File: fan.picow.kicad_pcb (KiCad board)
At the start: 2 copper layers, 96.5 x 70.6 mm, 61 parts, among them J1 12v Input, J12 Temp, J2 Fan1, J3 Fan2, J4 Fan4, J5 Fan3, J7 OLED, Q1 BSS138, Q2 BSS138, Q3 IRLML9301, SW1 EG1257, U1 PicoW, U3 LM2575

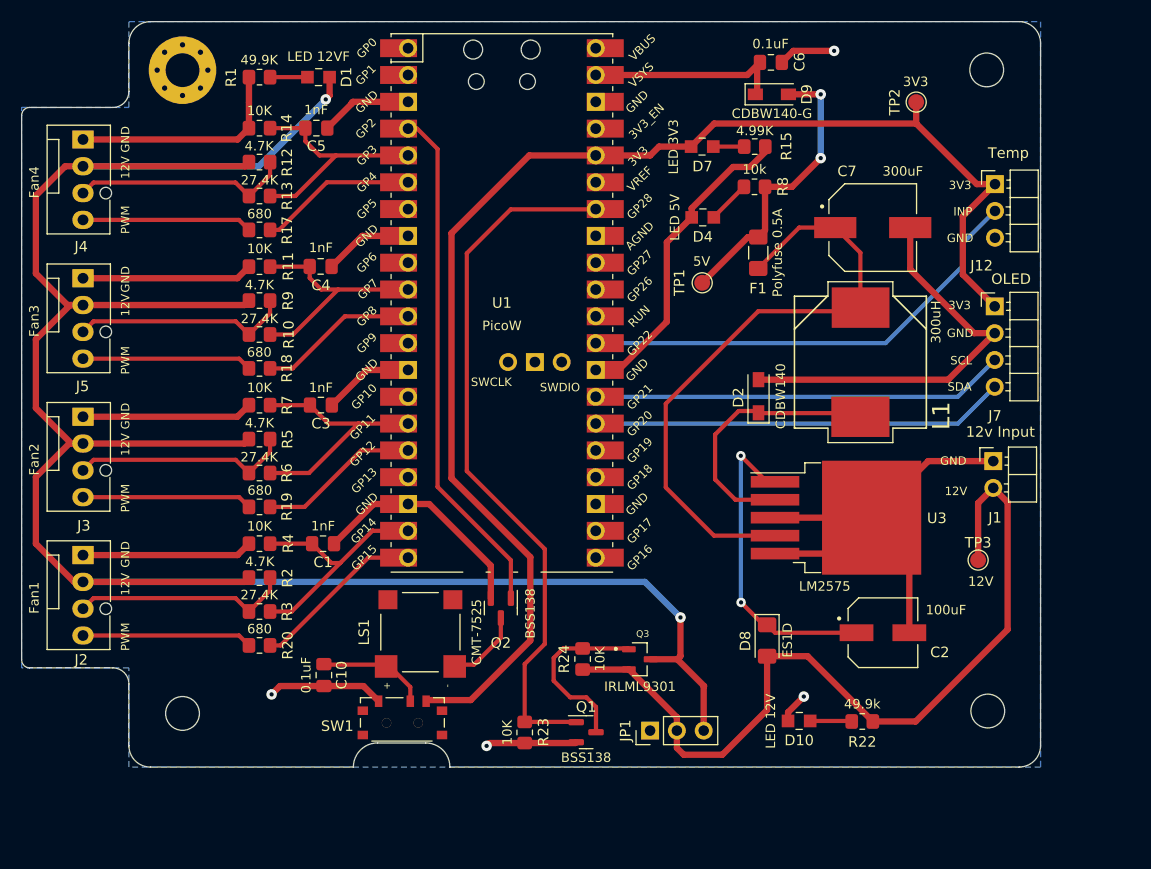
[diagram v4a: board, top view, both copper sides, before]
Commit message: back to rectangle shape
Move switch to the left
Move 12vf led to the bottom
Remove vias -redo part of the layout
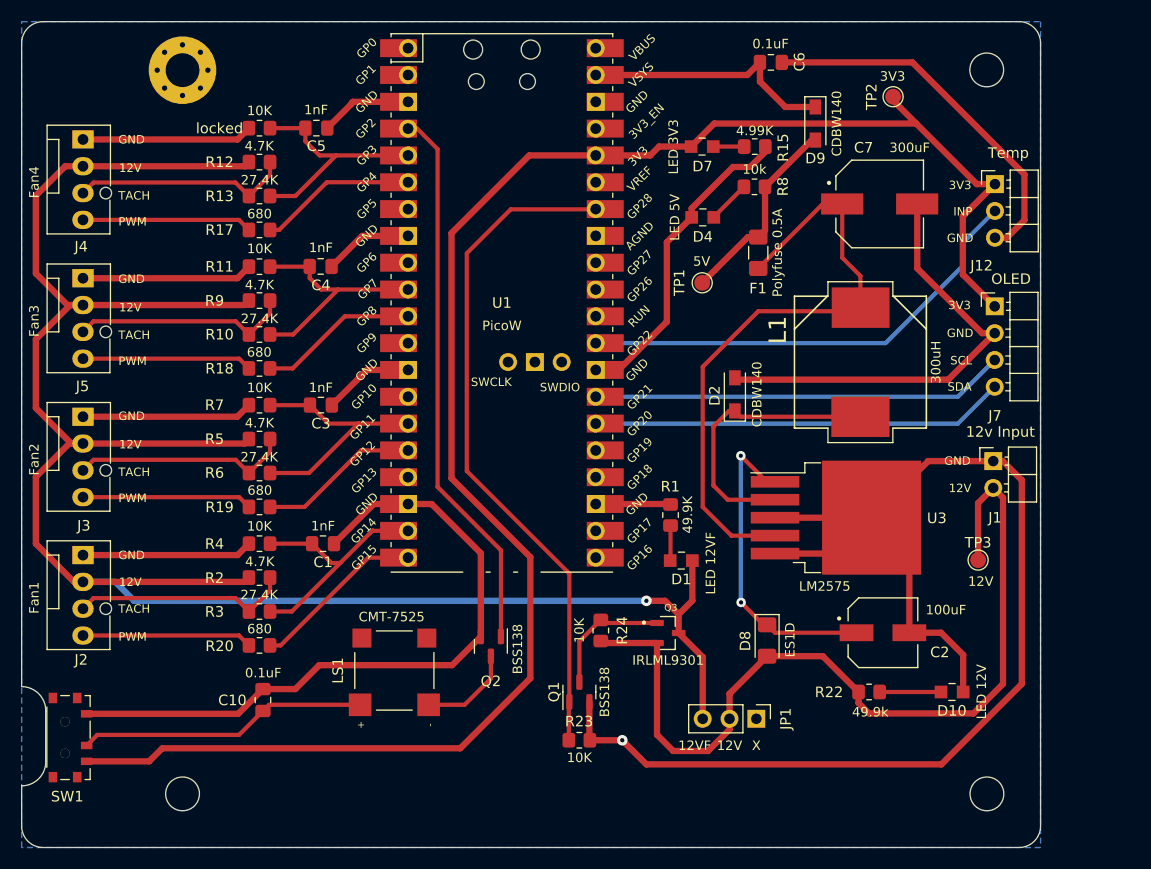
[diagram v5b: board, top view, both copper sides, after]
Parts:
- D9: value CDBW140-G -> CDBW140
- moved D1 57.3 mm to (156.5, 92.2)
- moved R1 56.9 mm to (155.4, 87.9), turned to 90 degrees
- moved SW1 32.3 mm to (97.8, 109.0), turned to -90 degrees
- moved D10 14.7 mm to (182.1, 104.6), turned to 0 degrees
- moved JP1 10.1 mm to (163.6, 107.2), turned to -90 degrees
- moved H3 7.85 mm to (185.4, 114.3)
- moved H2 7.62 mm to (109.2, 114.3)
- moved C10 6.23 mm to (116.8, 105.4), turned to 90 degrees
- moved R23 5.23 mm to (146.8, 109.2), turned to 0 degrees
- moved D9 4.96 mm to (169.2, 50.8), turned to -90 degrees
- moved LS1 4.39 mm to (129.3, 102.6)
- moved Q1 3.86 mm to (146.8, 104.6), turned to 90 degrees
- moved Q2 3.75 mm to (138.4, 100.3)
- moved Q3 3.65 mm to (155.2, 99.1)
- moved R24 3.20 mm to (148.8, 98.8)
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- renumbered R14 to locked
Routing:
- net GND: track 259.7 -> 397.6 mm, vias 4 -> 1
- net /3V3: track 128.2 -> 166.2 mm
- net /12VF: track 218.8 -> 192.7 mm, vias 2 -> 1
- net Net-(C10-Pad1): track 10.4 -> 27.5 mm
- net /5V: track 27.8 -> 18.7 mm, vias 2 -> 0
- net Net-(Q1-Pad3): track 17.1 -> 11.8 mm
- net /VSYS: track 19.2 -> 24.1 mm
- net /12V: track 79.7 -> 83.6 mm
- net /BUZZ: track 49.0 -> 52.3 mm
- net /RELC: track 67.1 -> 64.1 mm
- net Net-(D10-Pad1): track 3.96 -> 5.81 mm
- net Net-(LS1-PadN): track 7.48 -> 9.04 mm
- net Net-(D2-Pad1): track 25.5 -> 26.7 mm
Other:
- board size 96.5 x 70.6 mm -> 96.5 x 78.2 mm
- board text added: "12VF"
- board text added: "Fan Controller v0.3 Based on RaspberryPi PicoW MCU"
- board text added: "TACH"
- board text added: "X"
- board text added: "by Jaime Botella jimbotel@gmail.com 2023/04"
- board text removed: "Falta: - Tamaño de la placa (para caja standard) y posicion agujeros - Redondear los bordes (cambiar rectangulo por lineas)"
- board text removed: "Fan Controller v0.2 Based on RaspberryPi PicoW MCU"
- board text removed: "by Jaime Botella jimbotel@gmail.com 2023/03"

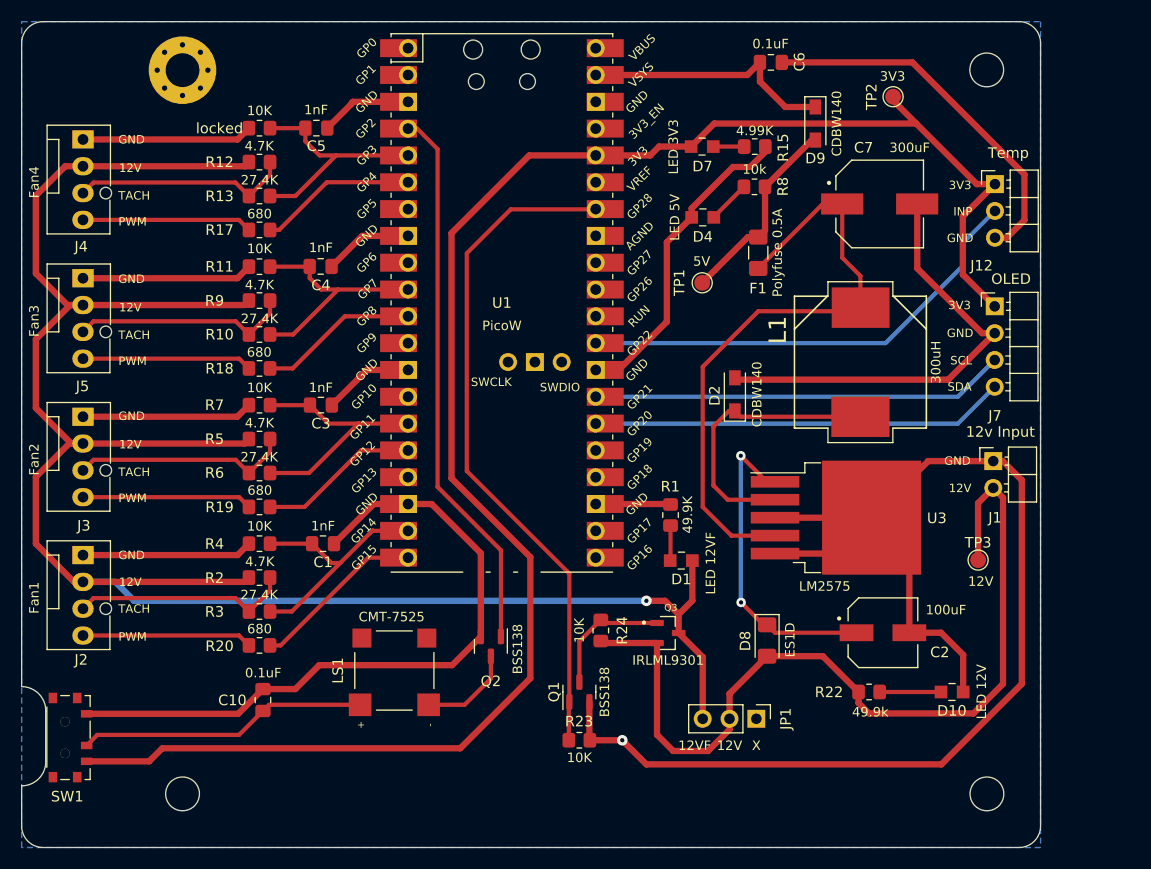
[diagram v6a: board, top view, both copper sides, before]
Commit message: Most SMD 1206 now
Also increase track size to 0.5 for Default subnet
And replace text so everything is more visible
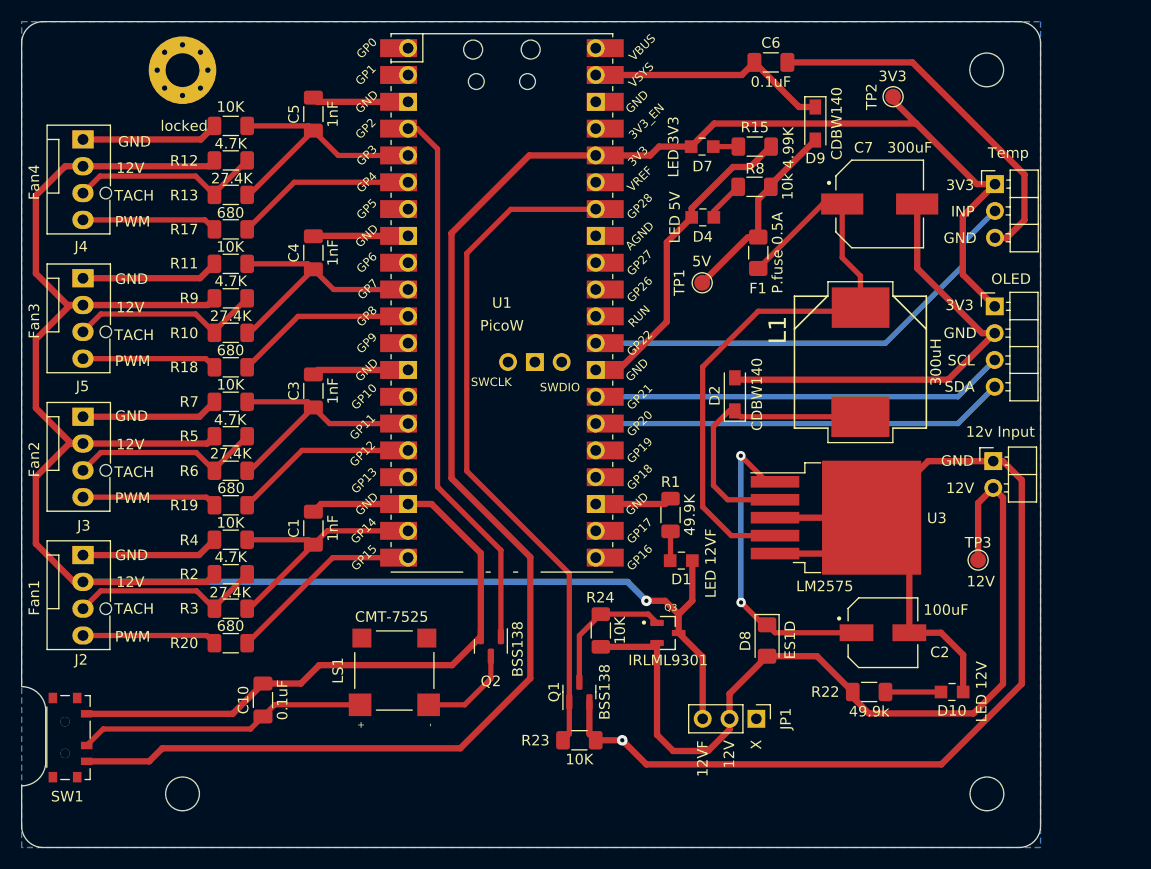
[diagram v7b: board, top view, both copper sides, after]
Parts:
- C1, C10, C3, C4, C5, C6: footprint Capacitor_SMD:C_0805_2012Metric_Pad1.18x1.45mm_HandSolder -> Capacitor_SMD:C_1206_3216Metric_Pad1.33x1.80mm_HandSolder
- F1: value Polyfuse 0.5A -> P.fuse 0.5A
- R1, R10, R11, R12, R13, R15, R17, R18, R19, R2, R20, R22, R23, R24, R3, R4, R5, R6, R7, R8, R9, locked: footprint Resistor_SMD:R_0805_2012Metric_Pad1.20x1.40mm_HandSolder -> Resistor_SMD:R_1206_3216Metric_Pad1.30x1.75mm_HandSolder
- moved R4 2.75 mm to (113.8, 90.2)
- moved R2 2.74 mm to (113.8, 93.5)
- moved R7 2.74 mm to (113.8, 77.2)
- moved R3 2.73 mm to (113.8, 96.8)
- moved R5 2.73 mm to (113.8, 80.4)
- moved R11 2.73 mm to (113.8, 64.1)
- moved R6 2.73 mm to (113.8, 83.7)
- moved R9 2.73 mm to (113.8, 67.4)
- moved locked 2.73 mm to (113.8, 51.0)
- moved R20 2.73 mm to (113.8, 100.0)
- moved R19 2.73 mm to (113.8, 87.0)
- moved R10 2.73 mm to (113.8, 70.6)
- moved R12 2.73 mm to (113.8, 54.3)
- moved R18 2.72 mm to (113.8, 73.9)
- moved R13 2.72 mm to (113.8, 57.6)
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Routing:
- net /12VF: track 192.7 -> 180.0 mm
- net GND: track 397.6 -> 386.9 mm
- net /PWMO1: track 16.1 -> 12.8 mm
- net /PWMO2: track 16.1 -> 12.8 mm
- net /PWMO3: track 16.1 -> 12.8 mm
- net /PWMO4: track 16.1 -> 12.8 mm
- net /TACHM4: track 22.7 -> 25.2 mm
- net /TACH1: track 20.7 -> 18.4 mm
- net /TACH4: track 20.7 -> 18.4 mm
- net /TACH2: track 20.7 -> 18.4 mm
- net /TACH3: track 20.7 -> 18.4 mm
- net /TACHM3: track 22.8 -> 25.0 mm
- net /PWM4: track 14.9 -> 17.1 mm
- net /PWM3: track 15.1 -> 17.2 mm
- net /PWM2: track 15.3 -> 17.4 mm
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
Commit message: move buzz switch to the border
also:
- Redo GND connections around LM2575
- Move some texts elements to make it neater
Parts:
- moved SW1 2.13 mm to (95.7, 108.9)
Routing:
- net GND: track 386.9 -> 416.0 mm
- net /3V3: track 166.2 -> 168.4 mm
- net Net-(C10-Pad1): track 27.5 -> 29.6 mm
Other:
- outline, holes or cut-outs redrawn
